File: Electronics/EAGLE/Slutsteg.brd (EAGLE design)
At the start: 100 x 160 mm, 181 parts, among them CN1 OSTYK33102030-2, CN2 OSTYK33102030-2, CN3 OSTYK33102030-2, IC1 SPX1117M3-L-3-3_TR, IC10 LM324D, IC11 L78M12ABDT-TR, IC2 L78M12ABDT-TR, IC3 ESP32-WROVER-IE-4MB, IC4 TM8211, IC5 LM324D, IC6 TPA3244DDWR, IC7 TPA3251D2DDVR, IC8 LM324D, IC9 LM324D, J1 0532610671, J2 JW-PJ-307-4H, J4 B4P-VH_LF__SN_, SW3 PDB181-K420F-103A2

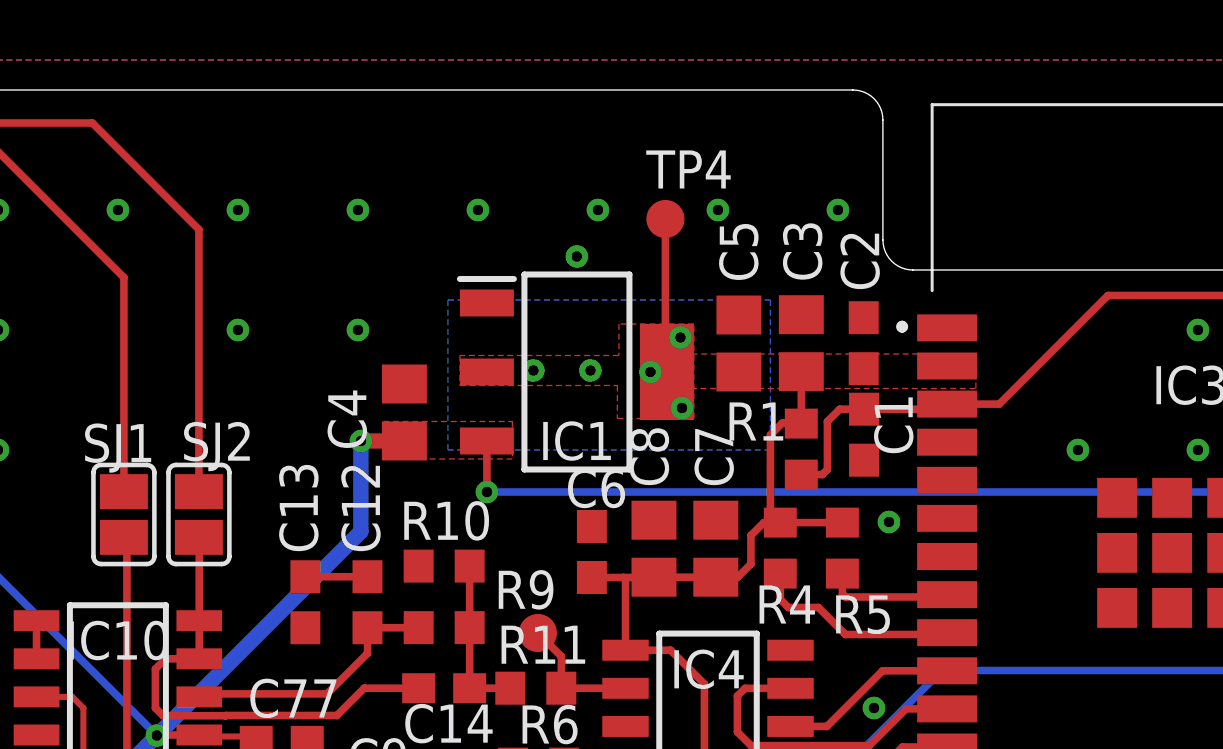
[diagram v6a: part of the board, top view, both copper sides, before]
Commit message: Added a header for the cooling fan.
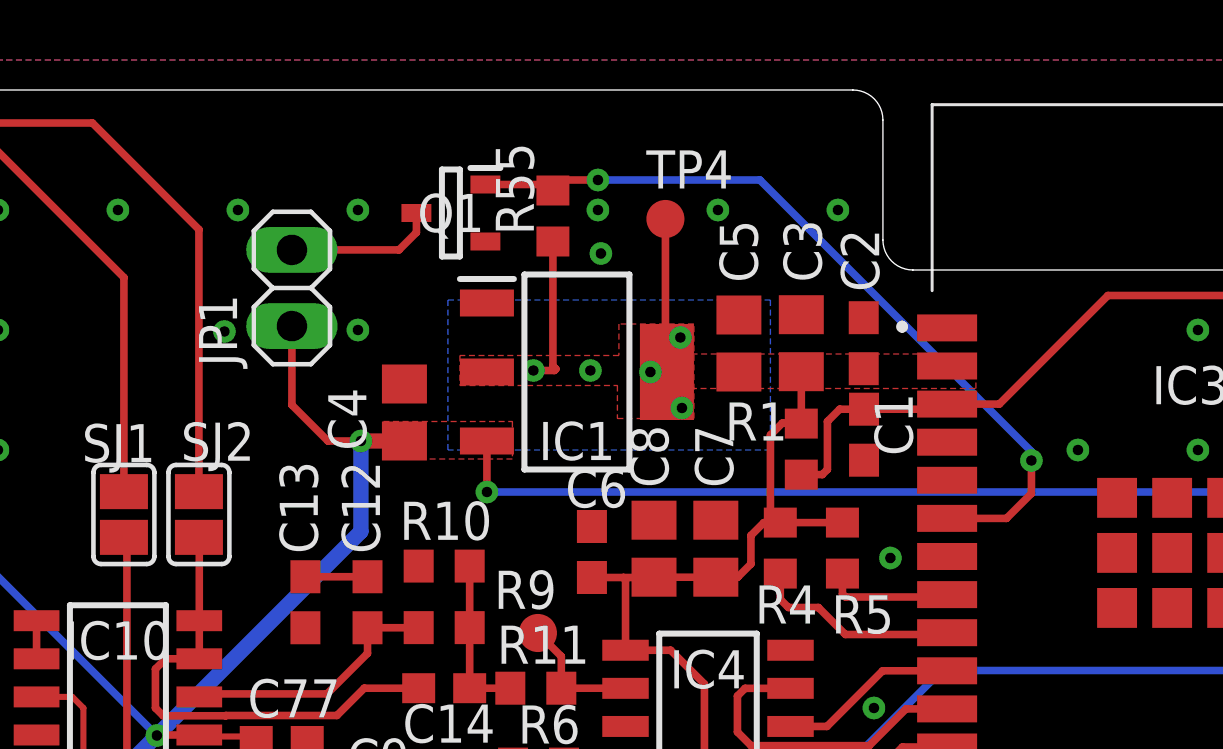
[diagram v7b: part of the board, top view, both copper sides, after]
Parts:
- added JP1: (no value), pinhead:1X02
- added Q1: RK7002BMT116, SamacSys_Parts:BSS64AHZGT116
- added R55: 10K/5%/0.1W, rcl:R0603
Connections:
- new net N$13: IC3.6, Q1.1, R55.2
- new net N$14: JP1.2, Q1.3
- net +3V3: now also R55.1
- net GND: now also Q1.2
- net VDD: now also JP1.1
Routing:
- net N$13: track 0.00 -> 26.7 mm, vias 0 -> 2
- net VDD: track 197.8 -> 203.2 mm
- net +3V3: track 117.3 -> 122.4 mm
- net N$14: track 0.00 -> 5.04 mm
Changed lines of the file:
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@@
 <drawing>
 <settings>
-<setting alwaysvectorfont="yes"/>
+<setting alwaysvectorfont="no"/>
 <setting verticaltext="up"/>
 </settings>
@@
 <element name="U$3" library="V5618A" package="V5618A" override_package3d_urn="urn:adsk.eagle:package:27391343/2" override_package_urn="urn:adsk.eagle:footprint:27391348/1" value="V5618A" x="25.85" y="45.4" locked="yes" smashed="yes" rot="MR90"/>
 <element name="U$4" library="V5618A" package="V5618A" override_package3d_urn="urn:adsk.eagle:package:27391343/2" override_package_urn="urn:adsk.eagle:footprint:27391348/1" value="V5618A" x="28.900290625" y="102.45" smashed="yes" rot="MR90"/>
+<element name="Q1" library="SamacSys_Parts" package="BSS64AHZGT116" value="RK7002BMT116" x="55.1" y="155.9" smashed="yes" rot="R180">
+<attribute name="ARROW_PART_NUMBER" value="" x="55.1" y="155.9" size="1.778" layer="27" rot="R180" display="off"/>
+<attribute name="ARROW_PRICE-STOCK" value="" x="55.1" y="155.9" size="1.778" layer="27" rot="R180" display="off"/>
+<attribute name="DESCRIPTION" value="2.5V Drive Nch MOSFET: MOSFETs are made as ultra-low ON-resistance by the micro-processing technologies suitable for mobilr equipment for low current consumption. In wide lineup including compact type, high-power type and complex type to meet in  the market." x="55.1" y="155.9" size="1.778" layer="27" rot="R180" display="off"/>
+<attribute name="HEIGHT" value="1.2mm" x="55.1" y="155.9" size="1.778" layer="27" rot="R180" display="off"/>
+<attribute name="MANUFACTURER_NAME" value="ROHM Semiconductor" x="55.1" y="155.9" size="1.778" layer="27" rot="R180" display="off"/>
+<attribute name="MANUFACTURER_PART_NUMBER" value="RK7002BMT116" x="55.1" y="155.9" size="1.778" layer="27" rot="R180" display="off"/>
+<attribute name="MOUSER_PART_NUMBER" value="755-RK7002BMT116" x="55.1" y="155.9" size="1.778" layer="27" rot="R180" display="off"/>
+<attribute name="MOUSER_PRICE-STOCK" value="https://www.mouser.co.uk/ProductDetail/ROHM-Semiconductor/RK7002BMT116?qs=npTsUczJOtO4aXz%2Fx%2FNVUw%3D%3D" x="55.1" y="155.9" size="1.778" layer="27" rot="R180" display="off"/>
+<attribute name="NAME" x="55.1" y="155.9" size="1.27" layer="25" rot="R180" align="center"/>
+<attribute name="VALUE" x="55.1" y="155.9" size="1.27" layer="27" rot="R180" align="center"/>
+</element>
+<element name="R55" library="rcl" library_urn="urn:adsk.eagle:library:334" package="R0603" package3d_urn="urn:adsk.eagle:package:23555/3" value="10K/5%/0.1W" x="58.5" y="155.8" smashed="yes" rot="R90">
+<attribute name="NAME" x="57.865" y="155.165" size="1.27" layer="25" rot="R90"/>
+<attribute name="POPULARITY" value="70" x="58.5" y="155.8" size="1.778" layer="27" rot="R90" display="off"/>
+<attribute name="SPICEPREFIX" value="R" x="58.5" y="155.8" size="1.778" layer="27" rot="R90" display="off"/>
+<attribute name="VALUE" x="60.405" y="155.165" size="1.27" layer="27" rot="R90"/>
+</element>
+<element name="JP1" library="pinhead" library_urn="urn:adsk.eagle:library:325" package="1X02" package3d_urn="urn:adsk.eagle:package:22435/2" value="" x="49.8" y="153.4" smashed="yes" rot="R90">
+<attribute name="NAME" x="47.9712" y="150.7838" size="1.27" layer="25" ratio="10" rot="R90"/>
+<attribute name="POPULARITY" value="98" x="49.8" y="153.4" size="1.778" layer="27" rot="R90" display="off"/>
+<attribute name="VALUE" x="52.975" y="150.86" size="1.27" layer="27" rot="R90"/>
+</element>
 </elements>
 <signals>
@@
 <vertex x="37.15" y="59"/>
 </polygon>
-<via x="69.7" y="145.6" extent="1-16" drill="0.35"/>
+<via x="69.75" y="144.4" extent="1-16" drill="0.35"/>
 <contactref element="R48" pad="1"/>
 <contactref element="IC5" pad="11"/>
@@
 <via x="44" y="156" extent="1-16" drill="0.35"/>
 <via x="52" y="156" extent="1-16" drill="0.35"/>
-<via x="56" y="156" extent="1-16" drill="0.35"/>
 <via x="60" y="156" extent="1-16" drill="0.35"/>
 <via x="64" y="156" extent="1-16" drill="0.35"/>
@@
 <via x="32" y="152" extent="1-16" drill="0.35"/>
 <via x="40" y="152" extent="1-16" drill="0.35"/>
-<via x="48" y="152" extent="1-16" drill="0.35"/>
+<via x="47.55" y="151.95" extent="1-16" drill="0.35"/>
 <via x="52" y="152" extent="1-16" drill="0.35"/>
-<via x="59.3" y="154.45" extent="1-16" drill="0.35"/>
+<via x="60.1" y="154.55" extent="1-16" drill="0.35"/>
 <via x="96" y="148" extent="1-16" drill="0.35"/>
 <via x="96" y="144" extent="1-16" drill="0.35"/>
@@
 <via x="16.6" y="102.6" extent="1-16" drill="0.35"/>
 <via x="18" y="102.6" extent="1-16" drill="0.35"/>
+<contactref element="Q1" pad="2"/>
 </signal>
 <signal name="PVDD">
@@
 <wire x1="37.4" y1="112.9" x2="37.4" y2="110.825" width="0.254" layer="1"/>
 <wire x1="37.4" y1="110.825" x2="37.425" y2="110.8" width="0.254" layer="1"/>
+<contactref element="JP1" pad="1"/>
+<wire x1="52.1" y1="148.3" x2="51" y2="148.3" width="0.254" layer="1"/>
+<wire x1="49.8" y1="149.5" x2="49.8" y2="152.13" width="0.254" layer="1"/>
+<wire x1="51" y1="148.3" x2="49.8" y2="149.5" width="0.254" layer="1"/>
 </signal>
 <signal name="SPEAKER_B_0">
@@
 <vertex x="55" y="148"/>
 </polygon>
+<contactref element="R55" pad="1"/>
+<wire x1="58.5" y1="154.95" x2="58.5" y2="150.8" width="0.254" layer="1"/>
+<wire x1="58.5" y1="150.8" x2="58.6" y2="150.7" width="0.254" layer="1"/>
+<wire x1="58.6" y1="150.7" x2="58.55" y2="150.65" width="0.254" layer="1"/>
+<wire x1="58.55" y1="150.65" x2="57.85" y2="150.65" width="0.254" layer="1"/>
 </signal>
 <signal name="N$59">
@@
 </polygon>
 </signal>
+<signal name="N$13">
+<contactref element="R55" pad="2"/>
+<contactref element="Q1" pad="1"/>
+<contactref element="IC3" pad="6"/>
+<wire x1="56.25" y1="156.85" x2="58.3" y2="156.85" width="0.254" layer="1"/>
+<wire x1="58.3" y1="156.85" x2="58.5" y2="156.65" width="0.254" layer="1"/>
+<wire x1="58.5" y1="156.65" x2="58.85" y2="157" width="0.254" layer="1"/>
+<wire x1="58.85" y1="157" x2="60" y2="157" width="0.254" layer="1"/>
+<via x="60" y="157" extent="1-16" drill="0.35"/>
+<via x="74.45" y="147.65" extent="1-16" drill="0.35"/>
+<wire x1="74.45" y1="147.65" x2="74.45" y2="146.55" width="0.254" layer="1"/>
+<wire x1="74.45" y1="146.55" x2="73.62" y2="145.72" width="0.254" layer="1"/>
+<wire x1="71.64" y1="145.72" x2="73.62" y2="145.72" width="0.254" layer="1"/>
+<wire x1="74.45" y1="147.65" x2="74.45" y2="147.95" width="0.254" layer="16"/>
+<wire x1="65.4" y1="157" x2="60" y2="157" width="0.254" layer="16"/>
+<wire x1="74.45" y1="147.95" x2="65.4" y2="157" width="0.254" layer="16"/>
+</signal>
+<signal name="N$14">
+<contactref element="Q1" pad="3"/>
+<contactref element="JP1" pad="2"/>
+<wire x1="49.8" y1="154.67" x2="53.37" y2="154.67" width="0.254" layer="1"/>
+<wire x1="53.95" y1="155.25" x2="53.95" y2="155.9" width="0.254" layer="1"/>
+<wire x1="53.37" y1="154.67" x2="53.95" y2="155.25" width="0.254" layer="1"/>
+</signal>
 </signals>
